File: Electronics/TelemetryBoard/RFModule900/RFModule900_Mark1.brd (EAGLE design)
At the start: 100 x 80 mm, 115 parts, among them T1 DC08-73, T2 DC08-73, U1 TPS2561, U2 TPS2561, U4 LTC5505, U5 LTC5505, U6 MCP4728, U7 LMV321, Y1 30 Mhz

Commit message: Work in progress
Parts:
- removed C12, C18: 1uF, SparkFun-Capacitors:0402-CAP
- removed D1, D2: (no value), SparkFun-LED:LED-0603
- added C51, C52, C53, C54: 0.1uF, SparkFun-Capacitors:0402-CAP
- added C55, C56: 1uF, SparkFun-Capacitors:0402-CAP
- added D6, D8, D9: (no value), SparkFun-LED:LED-0603
- added JP4: (no value), SparkFun-Connectors:1X01
- added R22, R23: DNP, SparkFun-Resistors:0402-RES
- added R24: 5k, SparkFun-Resistors:0402-RES
- added R25, R26, R27: 100k, SparkFun-Resistors:0402-RES
- added SJ5: (no value), SparkFun-Passives:PAD-JUMPER-3-2OF3_NC_BY_TRACE_YES_SILK_FULL_BOX
- added U$11: SN74LVC1G14, RitLaunchInitiative:SOT23-5
- C14: device SparkFun-Capacitors:0402-CAP -> SparkFun-Capacitors:0805
- L2: device SparkFun-Passives:C0402 -> SparkFun-Passives:0603
- R10, R15, R5: value 5k -> 270
- R11: value 5k -> 220
- R16, R17: value 10k -> DNP
- R8, R9: value 5k -> 25.5k
- SJ1, SJ3, SJ4: device SparkFun-Passives:PAD-JUMPER-3-2OF3_NC_BY_TRACE_YES_SILK_LARGE -> SparkFun-Passives:PAD-JUMPER-3-2OF3_NC_BY_TRACE_YES_SILK_FULL_BOX
- U$4: value LP3984 -> LP3984_DNP
- moved C2 320.0 mm to (-87.6, -273.1), turned to 0 degrees
- moved C16 314.4 mm to (-87.6, -269.2)
- moved D3 297.2 mm to (-77.5, -257.8)
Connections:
- net PA_LOADSWITCH_ENABLE renamed PA_PWR_EN_BREAKER
- net PA_OVERRIDE renamed PA_BREAKER_OVERRIDE
- removed net PA_ENABLE: JP1.20, U$7.2
- removed net RADIO_ENABLE: JP1.18, R7.2, U$1.P$1, U1.P$4
- removed net STATUS_LED: JP1.16
- new net BUFF_TR_SWITCH_CTL: R16.1, U$11.4, U$5.1
- new net DAC_3V3: D8.A, SJ5.3, U1.P$8
- new net DAC_PWR_EN: U1.P$5
- new net DAC_PWR_FAULT: R26.1, U1.P$6
- new net N$18: JP4.1, U6.P$9
- new net N$50: D9.C, R12.2
- new net N$52: R17.1, U$5.3
- new net N$53: SJ4.3, SJ5.2
- new net PA_PWR_EN: U$7.2
- new net PA_PWR_FAULT: R27.1, U2.P$10, U2.P$6
- new net RADIO_PWR_EN: U1.P$4
- new net RADIO_PWR_FAULT: R25.1, U1.P$10
- new net RADIO_SHUTDOWN: R7.2, U$1.P$1
- net 3.3V: now also C51.1, C52.1, C53.1, R17.2, R22.2, R23.2, R25.2, R26.2, R27.2, SJ5.1, U$11.5; no longer SJ4.3
- net 5V: now also C54.2
- net GND: now also C51.2, C52.2, C53.2, C54.1, C55.2, C56.2, R24.1, U$11.3; no longer C12.2, C18.2
- net N$19: now also C16.1; no longer C2.1
- net N$30: now also D6.C; no longer D2.C
- net N$31: now also D8.C, R24.2; no longer D1.C, R12.2
- net N$4: now also C2.1; no longer C12.1
- net N_IRQ: no longer JP1.11
- net N_SEL: no longer JP1.19
- net PA_3V3: now also D6.A; no longer D2.A
- net PA_PWR_REF: now also C56.1; no longer C18.1
- net PA_PWR_SENSE: now also C55.1; no longer C16.1
- net PA_TEMP: no longer JP1.14
- net RADIO_3V3: now also D9.A; no longer D1.A
- net SCL: now also R22.1
- net SCLK: no longer JP1.13
- net SDA: now also R23.1
- net SDI: no longer JP1.17
- net SDO: no longer JP1.15
- net TR_SWITCH_CTL: no longer U$5.1, U$5.3

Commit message: changed to a 3.6v bus for main board power for amp
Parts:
- removed C48: 0.1uF, SparkFun-Capacitors:0402-CAP
- removed U7: LMV321, RitLaunchInitiative:SOT23-5
- added C12: 0.1uF, SparkFun-Capacitors:0402-CAP
- added R28: 10k, SparkFun-Resistors:0402-RES
- added U$16: 10k, RitLaunchInitiative:0402
- added U3: LM75B, RitLaunchInitiative:HWSON8
- JP1: value M10X2SPECIAL -> (none)
- JP2, JP3: value M05X2PTH -> (none)
- R12, R24: value 5k -> 270
- R13: value 10k -> 0
- R14, R21: value 5k -> DNP
- R20: value 5k -> 0
- moved R14 331.3 mm to (-87.6, -285.8), turned to 0 degrees
- moved R13 328.1 mm to (-87.6, -281.9), turned to 0 degrees
- moved R20 183.3 mm to (-87.6, -289.6)
- moved R21 183.3 mm to (-87.6, -293.4)
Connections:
- net N$51 renamed VSWR_BREAKER_STATE
- net PA_3V3 renamed PA_3V6
- new net 3.6V: C52.1, U2.P$2, U2.P$3
- net 3.3V: now also C12.2, R28.2, U3.P$8; no longer C48.1, C52.1, R13.2, U2.P$2, U2.P$3, U7.5
- net GND: now also C12.1, R14.2, R21.2, U$16.2, U3.P$4; no longer C48.2, R14.1, R21.1, U7.2
- net N$47: now also C55.1, R13.1, R4.2, U$2.P$23; no longer R20.2, U$6.3, U7.4
- net N$48: now also C56.1, R3.2, U$2.P$24; no longer R21.2, U7.3
- net PA_PWR_REF: now also R20.2, R21.1; no longer C56.1, R3.2, U$2.P$24
- net PA_PWR_SENSE: now also R13.2, R14.1; no longer C55.1, R4.2, U$2.P$23
- net PA_TEMP: now also R28.1, U$16.1; no longer R13.1, R14.2
- net RF_POWER_IN: now also U$6.3; no longer U7.1
- net SCL: now also U3.P$2
- net SDA: now also U3.P$1

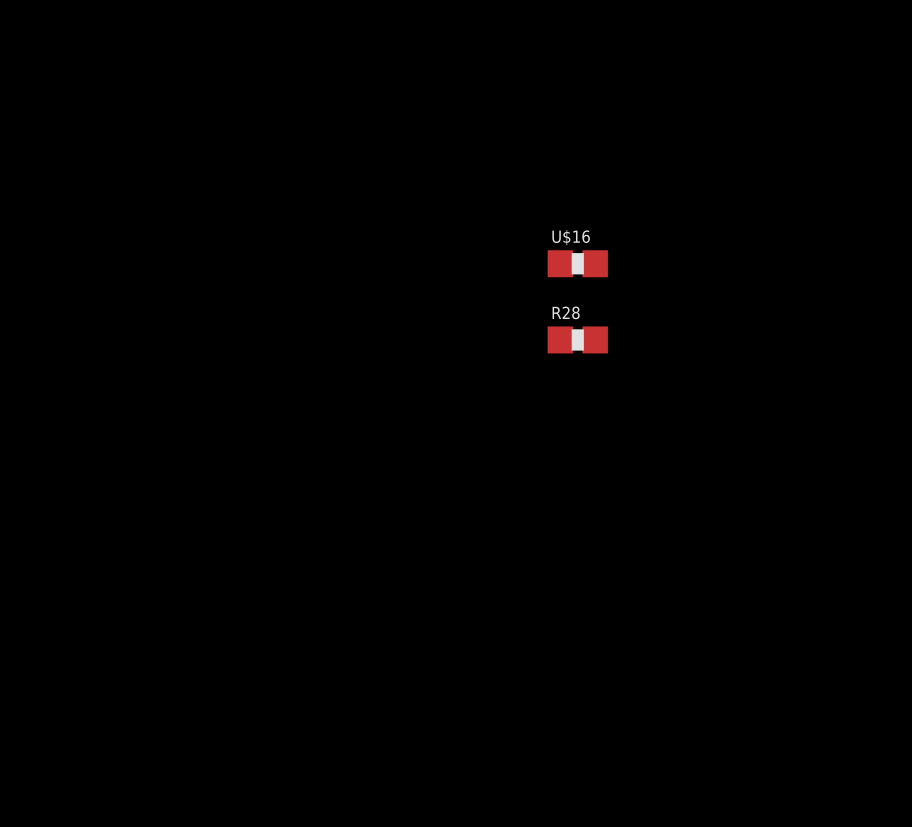
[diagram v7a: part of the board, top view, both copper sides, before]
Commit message: added new switching regulator
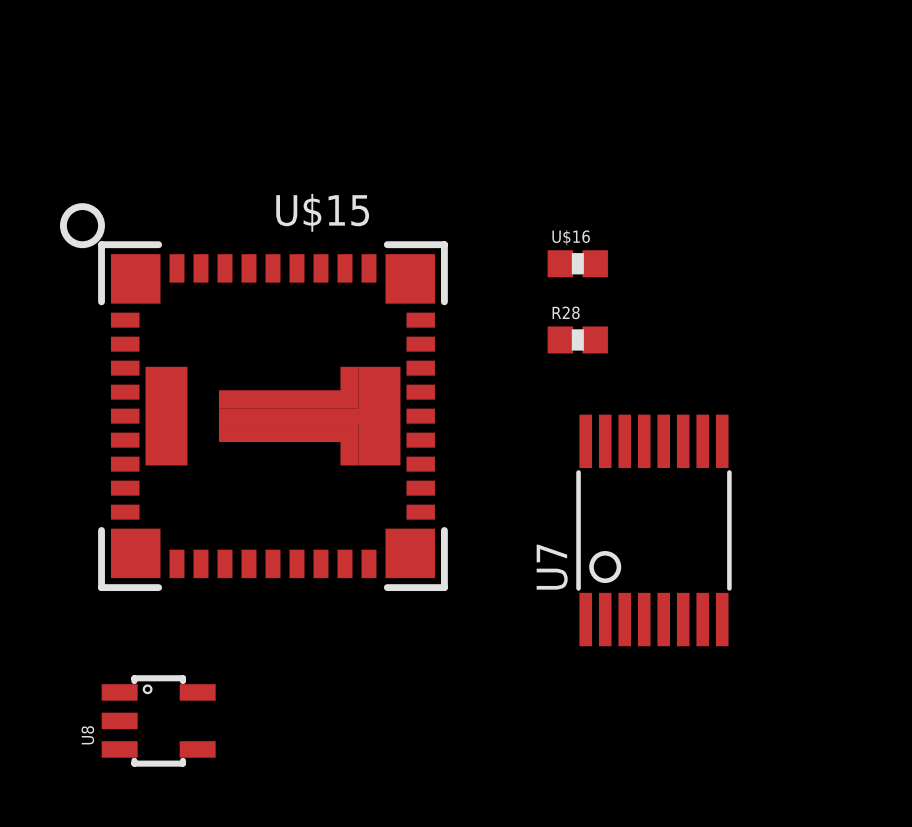
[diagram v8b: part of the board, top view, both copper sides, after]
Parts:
- added U$15: LMZ31704, RitLaunchInitiative:42-QFN
- added U7: ADC128D818, RitLaunchInitiative:16-TSSOP
- added U8: MIC5504-3.3YM5, RitLaunchInitiative:SOT23-5
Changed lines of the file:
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@@
 </element>
 <element name="R28" library="SparkFun-Resistors" package="0402-RES" value="10k" x="-87.63" y="-313.69"/>
+<element name="U7" library="RitLaunchInitiative" package="16-TSSOP" value="ADC128D818" x="-85.09" y="-320.04">
+<attribute name="DIGI" value="296-41182-1-ND" x="-85.09" y="-320.04" size="1.778" layer="27" display="off"/>
+<attribute name="MPN" value="ADC128D818CIMTX/NOPB" x="-85.09" y="-320.04" size="1.778" layer="27" display="off"/>
+</element>
+<element name="U$15" library="RitLaunchInitiative" package="42-QFN" value="LMZ31704" x="-97.79" y="-316.23">
+<attribute name="DIGI" value="296-37135-1-ND" x="-97.79" y="-316.23" size="1.778" layer="27" display="off"/>
+<attribute name="MPN" value="LMZ31704RVQT" x="-97.79" y="-316.23" size="1.778" layer="27" display="off"/>
+</element>
+<element name="U8" library="RitLaunchInitiative" package="SOT23-5" value="MIC5504-3.3YM5" x="-101.6" y="-326.39">
+<attribute name="DIGI" value="576-4764-1-ND" x="-101.6" y="-326.39" size="1.778" layer="27" display="off"/>
+<attribute name="MPN" value="MIC5504-3.3YM5 TR" x="-101.6" y="-326.39" size="1.778" layer="27" display="off"/>
+</element>
 </elements>
 <signals>
